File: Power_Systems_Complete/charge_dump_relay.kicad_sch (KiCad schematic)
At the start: 3 parts

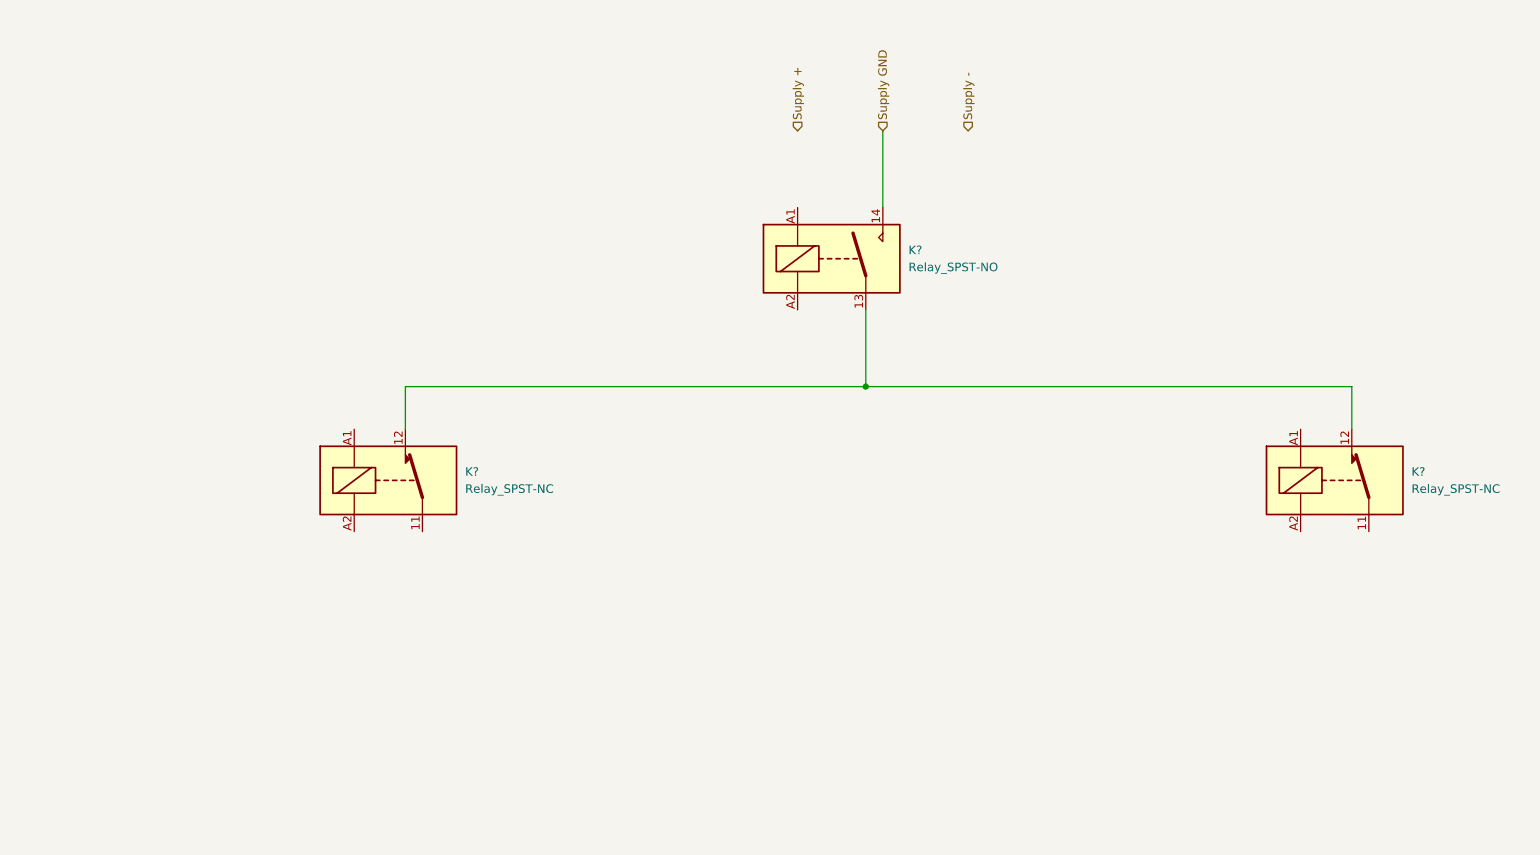
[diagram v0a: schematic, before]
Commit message: Added SPA to complete schematic
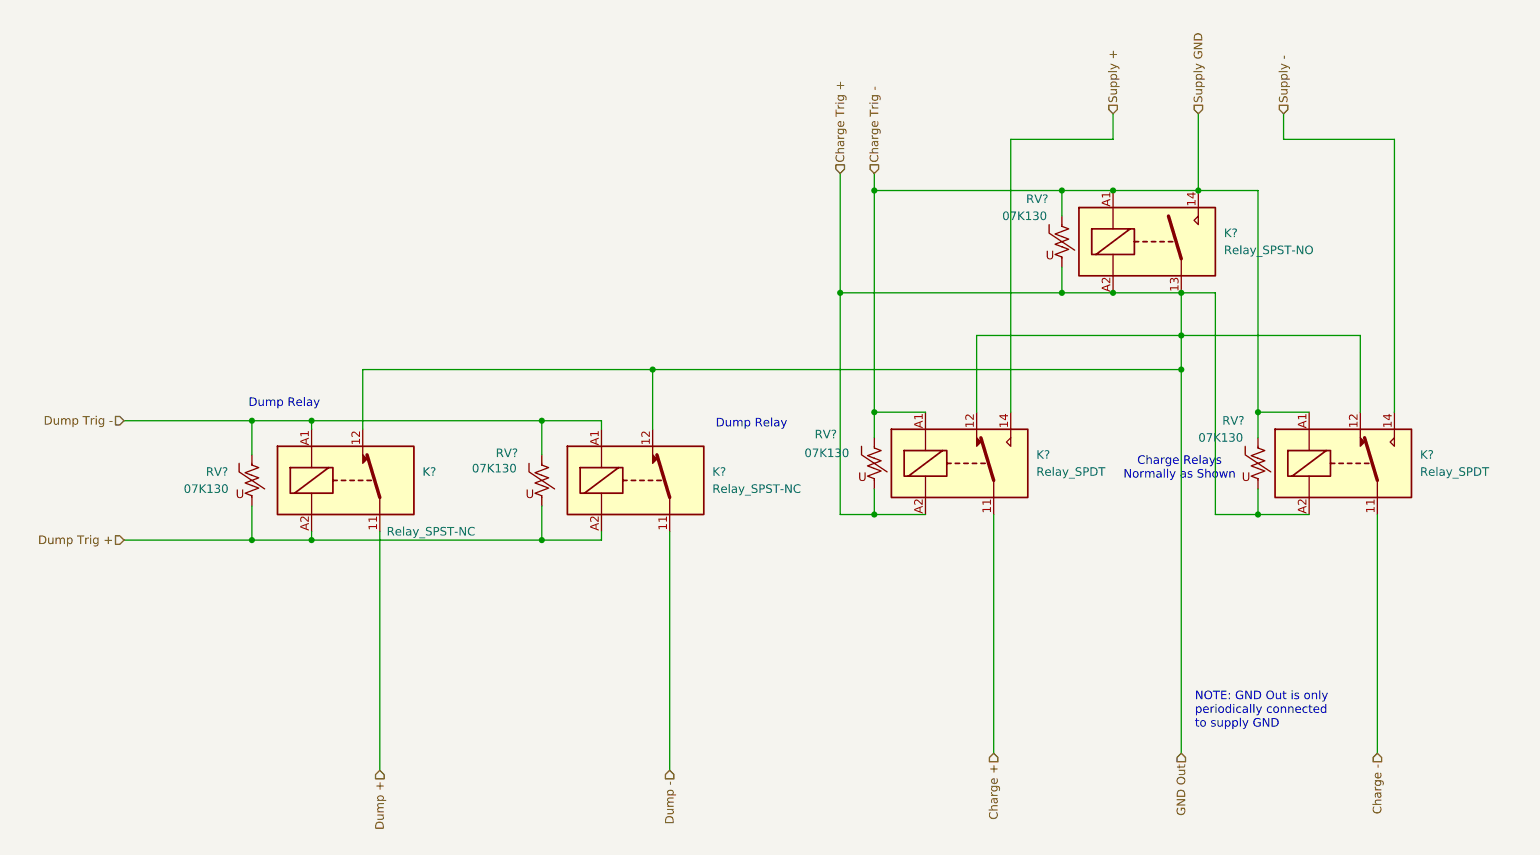
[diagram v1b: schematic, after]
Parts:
- added K? (x2): Relay_SPDT, symbol Relay:Relay_SPDT
- added RV? (x5): 07K130, symbol Device:Varistor_US
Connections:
- net Supply GND is gone; now on net Charge Trig -: K?.14
- net Supply +: now also K?.14
- net Supply -: now also K?.14
- net Dump -: now reaches K?.11
- net Charge Trig +: now reaches K?.12, K?.12, K?.13
- net Charge Trig +: now also K?.A2, K?.12, K?.12, K?.A2, K?.A2, RV?.2, RV?.2, RV?.2
- net Dump Trig -: now reaches K?.A1
- net Dump Trig -: now also K?.A1, RV?.1, RV?.1
- net Dump Trig +: now reaches K?.A2
- net Dump Trig +: now also K?.A2, RV?.2, RV?.2
- net Dump +: now reaches K?.11
- net Charge Trig -: now reaches K?.A1
- net Charge Trig -: now also K?.A1, K?.A1, RV?.1, RV?.1, RV?.1
- new net Charge +: K?.11
- new net Charge -: K?.11
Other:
- note added: "Charge Relays Normally as Shown"
- note added: "Dump Relay"
- note added: "NOTE: GND Out is only periodically connected to supply GND"
- moved on the sheet: K?
